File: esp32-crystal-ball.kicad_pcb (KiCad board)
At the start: 2 copper layers, 48.7 x 45 mm, 54 parts, among them J1 TYPE-C-31-M-12, J2 Barrel_Jack_Switch, J3 Screw_Terminal_01x03, J4 Conn_02x03_Counter_Clockwise, J5 Conn_01x02_Pin, Q1 NTA4151PT1G, U1 ESP32-S3-MINI-1, U2 OWMMOD-403010A-S261F, U3 NCP167BMX330TBG, U4 SN74LV1T34DBV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

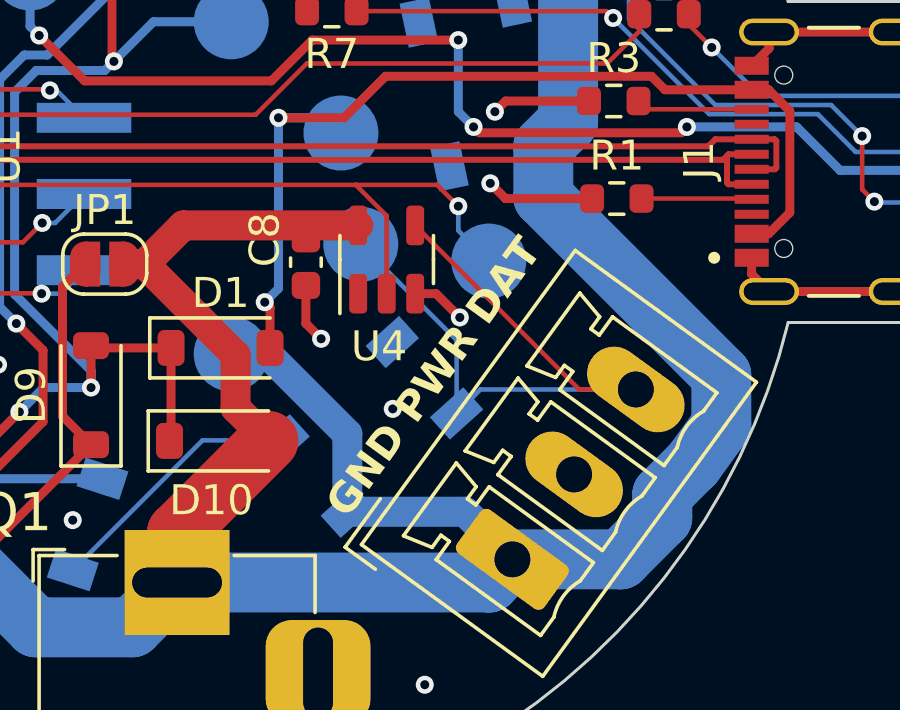
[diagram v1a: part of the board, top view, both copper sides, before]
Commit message: Fix silk screen
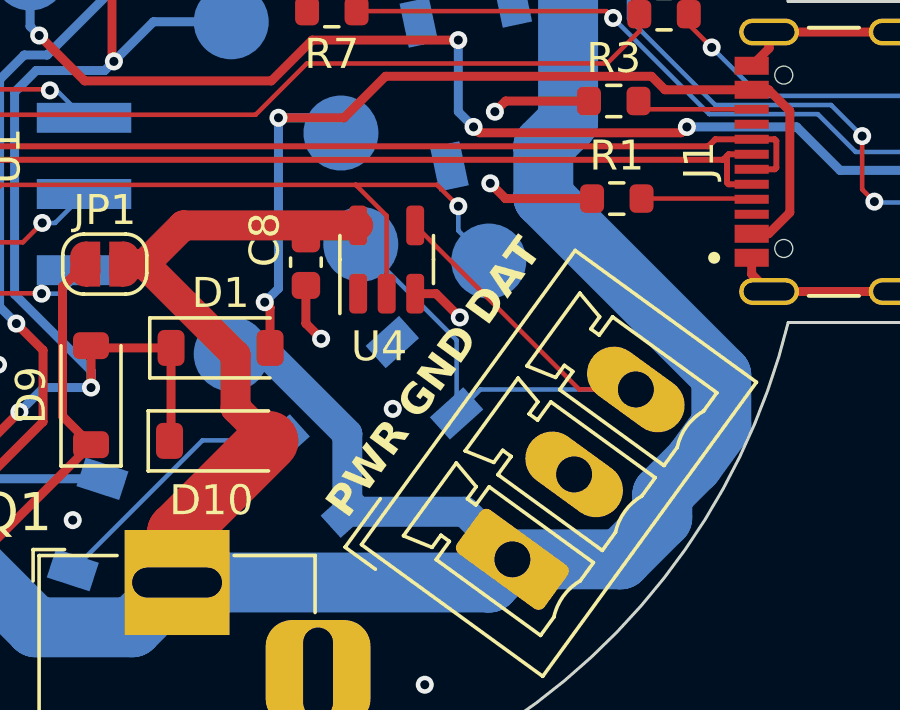
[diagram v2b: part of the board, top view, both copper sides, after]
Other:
- board text added: "PWR GND DAT"
- board text removed: "GND PWR DAT"
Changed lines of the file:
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@@
 		(fp_line
 			(start -3.65 2.75)
-			(end 3.65 2.749999)
+			(end 3.65 2.749998)
 			(stroke
 				(width 0.12)
@@
 		)
 		(fp_line
-			(start -3.65 -2.749999)
+			(start -3.65 -2.749998)
 			(end 3.65 -2.75)
 			(stroke
@@
 		)
 		(property "Value" "SK6812"
-			(at -0.000001 -3.999999 102)
+			(at -0.000002 -3.999999 102)
 			(layer "B.Fab")
 			(effects
@@
 		)
 		(fp_line
-			(start -3.65 -2.749999)
+			(start -3.65 -2.749998)
 			(end 3.65 -2.75)
 			(stroke
@@
 		(fp_line
 			(start -3.65 2.75)
-			(end 3.65 2.749999)
+			(end 3.65 2.749998)
 			(stroke
 				(width 0.12)
@@
 		)
 	)
-	(gr_text "GND PWR DAT"
+	(gr_text "PWR GND DAT"
 		(at 148.336 86.4108 54)
 		(layer "F.SilkS")
